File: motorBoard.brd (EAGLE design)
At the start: 127 x 76.3 mm, 74 parts

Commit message: Fixed Git Issues
If this push works, this should be the end of the git-astrophe.
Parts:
- removed C3: 0.1uF, eagle-ltspice:C1206
- moved C8 20.5 mm to (73.4, 9.40)
- moved OSC 19.3 mm to (68.1, 7.62), turned to 270 degrees
- moved C2 16.2 mm to (80.0, 19.7), turned to 0 degrees
- moved C1 2.67 mm to (95.2, 6.48)
- moved C6 1.52 mm to (93.2, 24.0)
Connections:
- net +3V3: now also U$1.73, U$1.74, U$1.75; no longer C3.2
- net +5V: now also U$1.1, U$1.2, U$1.3
- net GNDA: now also U$1.4, U$1.5, U$1.6, U$1.76, U$1.77, U$1.78; no longer C3.1
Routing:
- net MOTOR2A1: track 168.3 -> 105.2 mm, vias 4 -> 3
- net BASIC_HEADER1-4: track 141.6 -> 79.5 mm, vias 5 -> 4
- net MOTOR2LIMB: track 118.0 -> 62.2 mm, vias 2 -> 3
- net MOTOR1POT: track 138.4 -> 89.5 mm, vias 3 -> 4
- net BASIC_HEADER1-5: track 127.2 -> 81.3 mm
- net BASIC_HEADER2-2: track 128.4 -> 91.6 mm, vias 3 -> 4
- net BASIC_HEADER2-4: track 130.3 -> 95.5 mm
- net +5V: track 360.3 -> 326.3 mm, vias 12 -> 8
- net BASIC_HEADER2-6: track 136.7 -> 109.6 mm, vias 9 -> 4
- net BASIC_HEADER2-3: track 118.7 -> 93.4 mm
- net MOTOR4LIMA: track 43.6 -> 68.5 mm, vias 1 -> 2
- net MOTOR1LIMA: track 111.6 -> 88.7 mm, vias 2 -> 3
- net MOTOR4A1: track 82.5 -> 62.0 mm, vias 1 -> 3
- net MOTOR4LIMB: track 36.8 -> 55.6 mm
- net +3V3: track 485.1 -> 503.4 mm, vias 5 -> 2
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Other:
- board text added: "3.3V"
- board text added: "5V"
- board text added: "GND"

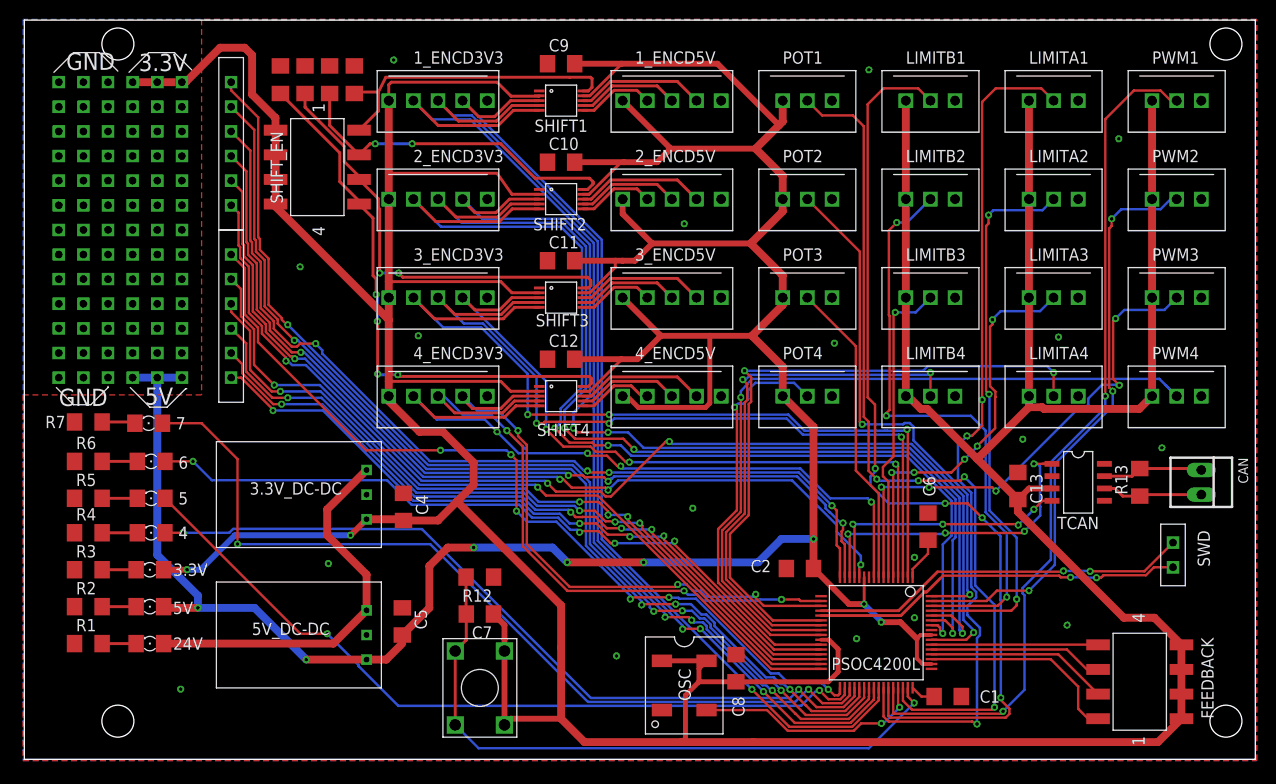
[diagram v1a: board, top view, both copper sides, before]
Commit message: Mostly done with the small board
Removed 1 motor channel, all 3V3 encoders, level shifter enable switches, 1 gpio header. Moved around a ton of components.
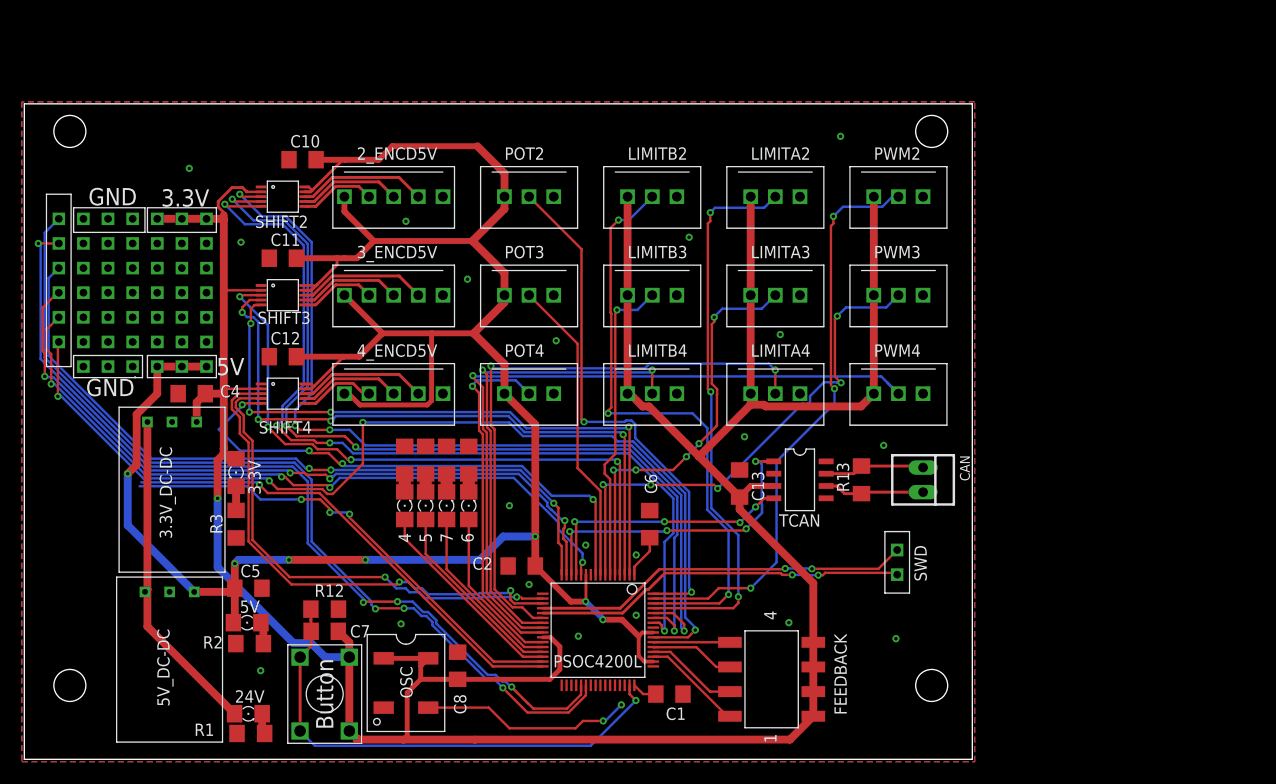
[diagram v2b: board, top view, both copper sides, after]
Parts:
- removed 1_ENCD3V3, 1_ENCD5V, 2_ENCD3V3, 3_ENCD3V3, 4_ENCD3V3: MOLEX5, HuskyRobotics2017-18:MOLEX22-23-2051
- removed BASIC_HEADER1: 6BASIC_HEADER, HuskyRobotics2017-18:6SIP_HEADER
- removed C9: 0.1uF, eagle-ltspice:C1206
- removed LIMITA1, LIMITB1, POT1, PWM1: MOLEX3, HuskyRobotics2017-18:MOLEX22-23-2031
- removed R10, R11, R8, R9: 4.7k, eagle-ltspice:R1206
- removed SHIFT1: LEVEL-SHIFTER_NVT2003DPNVT_2003DP_LEVEL_SHIFTER, HuskyRobotics2017-18:TSSOP10
- removed SHIFT_EN: SMD4SWSMD4SW, HuskyRobotics2017-18:GULL8
- removed U$2: PUSH_BUTTON, HuskyRobotics2017-18:PUSH_BUTTON
- added BUTTON: PUSH_BUTTON, HuskyRobotics2017-18:PUSH_BUTTON
- U$1: value OOPS_SPACE -> OOPS_SPACESMALL; device HuskyRobotics2017-18:OOPS_SPACE -> HuskyRobotics2017-18:OOPS_SPACE_SMALL
- moved R6 39.2 mm to (45.8, 30.9), turned to 270 degrees
- moved FEEDBACK 38.0 mm to (77.1, 8.26)
- moved R7 37.2 mm to (43.6, 30.9), turned to 270 degrees
- moved R5 35.0 mm to (41.4, 30.9), turned to 270 degrees
- moved R4 33.5 mm to (39.2, 30.9), turned to 270 degrees
- moved 6 33.1 mm to (45.8, 26.2), turned to 90 degrees
- moved 7 31.9 mm to (43.6, 26.2), turned to 90 degrees
- moved CAN 28.7 mm to (92.7, 28.8)
- moved 2_ENCD5V 28.7 mm to (38.1, 58.0)
- moved 3_ENCD5V 28.7 mm to (38.1, 47.9)
- moved 4_ENCD5V 28.7 mm to (38.1, 37.7)
- moved C2 28.7 mm to (51.3, 19.9)
- moved C8 28.7 mm to (44.7, 9.65)
- moved OSC 28.7 mm to (39.4, 7.87)
- moved POT2 28.7 mm to (52.1, 58.0)
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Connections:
- removed net BASIC_HEADER1-1: BASIC_HEADER1.1, PSOC4200L.28
- removed net BASIC_HEADER1-2: BASIC_HEADER1.2, PSOC4200L.29
- removed net BASIC_HEADER1-3: BASIC_HEADER1.3, PSOC4200L.30
- removed net BASIC_HEADER1-6: BASIC_HEADER1.6, PSOC4200L.33
- removed net LEVEL_SHIFT_EN1: R11.2, SHIFT1.10, SHIFT_EN.8
- removed net LEVEL_SHIFT_EN2: R10.2, SHIFT2.10, SHIFT_EN.7
- removed net LEVEL_SHIFT_EN3: R9.2, SHIFT3.10, SHIFT_EN.6
- removed net LEVEL_SHIFT_EN4: R8.2, SHIFT4.10, SHIFT_EN.5
- removed net MOTOR1A1: 1_ENCD3V3.4, PSOC4200L.41, SHIFT1.3
- removed net MOTOR1A2: 1_ENCD3V3.3, PSOC4200L.40, SHIFT1.4
- removed net MOTOR1A3: 1_ENCD3V3.2, PSOC4200L.39, SHIFT1.5
- removed net MOTOR1B1: 1_ENCD5V.4, SHIFT1.8
- removed net MOTOR1B2: 1_ENCD5V.3, SHIFT1.7
- removed net MOTOR1B3: 1_ENCD5V.2, SHIFT1.6
- removed net MOTOR1LIMA: LIMITA1.2, PSOC4200L.42
- removed net MOTOR1LIMB: LIMITB1.2, PSOC4200L.43
- removed net MOTOR1POT: POT1.2, PSOC4200L.46
- removed net MOTOR1PWM: PSOC4200L.44, PWM1.2
- net +3V3: now also BUTTON.B1, BUTTON.B2, U$1.37, U$1.38, U$1.39; no longer 1_ENCD3V3.1, 2_ENCD3V3.1, 3_ENCD3V3.1, 4_ENCD3V3.1, LIMITA1.1, LIMITB1.1, PWM1.1, SHIFT1.2, SHIFT_EN.1, SHIFT_EN.2, SHIFT_EN.3, SHIFT_EN.4, U$1.73, U$1.74, U$1.75, U$2.B1, U$2.B2
- net +5V: now also SHIFT2.10, SHIFT3.10, SHIFT4.10; no longer 1_ENCD5V.1, C9.2, POT1.1, SHIFT1.9
- net BASIC_HEADER1-4: no longer BASIC_HEADER1.4
- net BASIC_HEADER1-5: no longer BASIC_HEADER1.5
- net CLK_EXT: no longer PSOC4200L.45
- net GNDA: now also U$1.40, U$1.41, U$1.42; no longer 1_ENCD3V3.5, 1_ENCD5V.5, 2_ENCD3V3.5, 3_ENCD3V3.5, 4_ENCD3V3.5, C9.1, LIMITA1.3, LIMITB1.3, POT1.3, PWM1.3, R10.1, R11.1, R8.1, R9.1, SHIFT1.1, U$1.76, U$1.77, U$1.78
- net LED4: now also PSOC4200L.30; no longer PSOC4200L.36
- net LED5: now also PSOC4200L.29; no longer PSOC4200L.34
- net LED7: now also PSOC4200L.28; no longer PSOC4200L.35
- net MOTOR2A1: no longer 2_ENCD3V3.4
- net MOTOR2A2: no longer 2_ENCD3V3.3
- net MOTOR2A3: no longer 2_ENCD3V3.2
- net MOTOR3A1: no longer 3_ENCD3V3.4
- net MOTOR3A2: no longer 3_ENCD3V3.3
- net MOTOR3A3: no longer 3_ENCD3V3.2
- net MOTOR4A1: no longer 4_ENCD3V3.4
- net MOTOR4A2: no longer 4_ENCD3V3.3
- net MOTOR4A3: no longer 4_ENCD3V3.2
- net XRES: now also BUTTON.A1, BUTTON.A2; no longer U$2.A1, U$2.A2
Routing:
- net +3V3: track 503.4 -> 304.2 mm, vias 2 -> 1
- net MOTOR1A3: track 108.8 -> 0.00 mm, vias 3 -> 0
- net MOTOR1A2: track 104.1 -> 0.00 mm, vias 3 -> 0
- net MOTOR1A1: track 99.5 -> 0.00 mm, vias 1 -> 0
- net MOTOR1LIMB: track 97.5 -> 0.00 mm, vias 4 -> 0
- net MOTOR1POT: track 89.5 -> 0.00 mm, vias 4 -> 0
- net BASIC_HEADER1-6: track 89.4 -> 0.00 mm, vias 6 -> 0
- net MOTOR1PWM: track 88.7 -> 0.00 mm, vias 2 -> 0
- net MOTOR1LIMA: track 88.7 -> 0.00 mm, vias 3 -> 0
- net BASIC_HEADER1-3: track 76.9 -> 0.00 mm, vias 4 -> 0
- net +5V: track 326.3 -> 251.2 mm, vias 8 -> 7
- net BASIC_HEADER1-2: track 74.5 -> 0.00 mm, vias 4 -> 0
- net BASIC_HEADER1-1: track 72.8 -> 0.00 mm, vias 4 -> 0
- net LED7: track 90.2 -> 18.4 mm, vias 2 -> 0
- net LED5: track 81.0 -> 19.8 mm, vias 2 -> 0
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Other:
- board size 127 x 76.3 mm -> 97.8 x 67.6 mm
- board text added: "Button"
- board text removed: "R8...11"

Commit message: "Done" except for silk screen and DFM check
Added 24V terminal blocks, second CAN header, limit switch debounces.
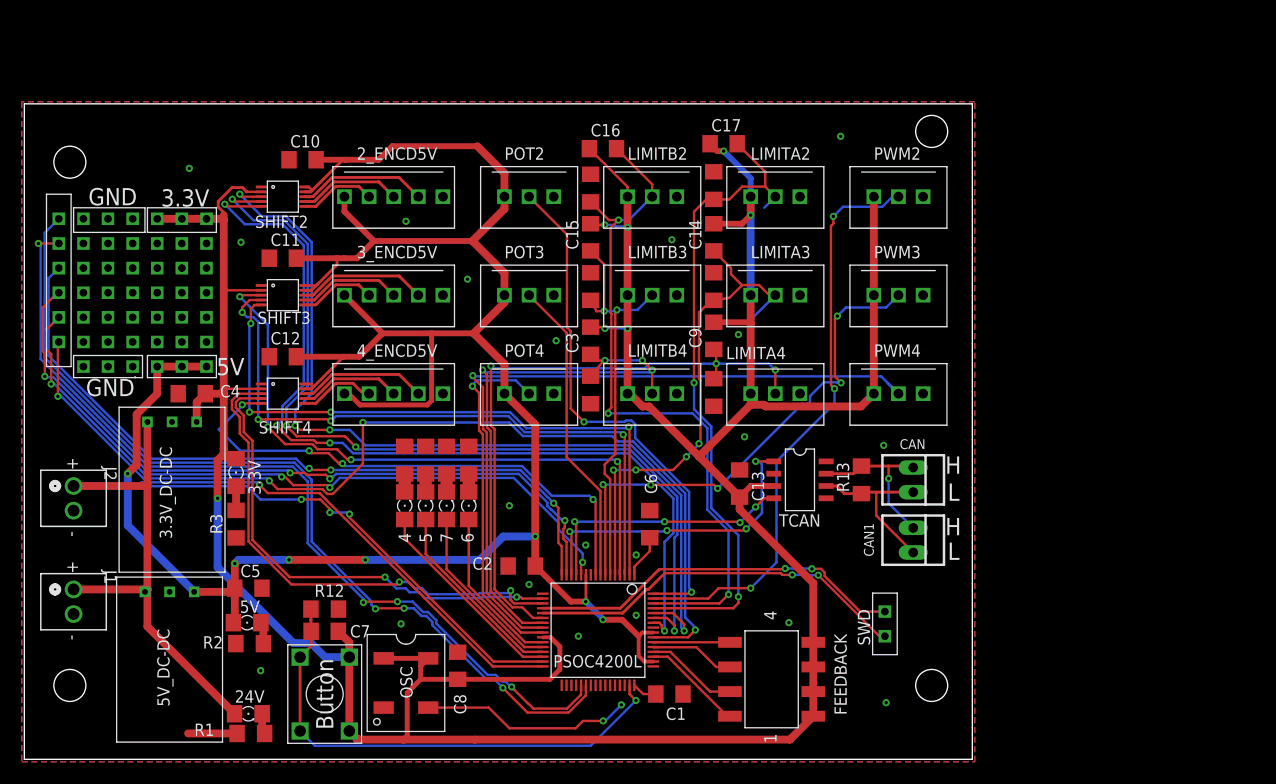
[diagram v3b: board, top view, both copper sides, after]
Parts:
- added C14, C15, C16, C17, C3, C9: 0.1uF, eagle-ltspice:C1206
- added CAN1: 22-23-2021, con-molex:22-23-2021
- added J1, J2: TE-TERM-BLOCK, HuskyRobotics17-18:TE-TERM-BLOCK
- added R10, R11, R14, R15, R8, R9: 1k, eagle-ltspice:R1206
- moved SWD 6.48 mm to (88.8, 14.0)
- moved CAN 1.02 mm to (91.7, 28.8)
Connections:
- net +24V: now also J1.L, J2.L
- net +3V3: now also C14.2, C15.2, C16.1, C17.1, C3.2, C9.2
- net CANH: now also CAN1.1
- net CANL: now also CAN1.2
- net GNDA: now also J1.R, J2.R, R10.1, R11.1, R14.1, R15.1, R8.1, R9.1
- net MOTOR2LIMA: now also C17.2, R14.2
- net MOTOR2LIMB: now also C16.2, R15.2
- net MOTOR3LIMA: now also C14.1, R11.2
- net MOTOR3LIMB: now also C15.1, R10.2
- net MOTOR4LIMA: now also C9.1, R9.2
- net MOTOR4LIMB: now also C3.1, R8.2
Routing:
- net +3V3: track 304.2 -> 334.3 mm, vias 1 -> 7
- net +24V: track 34.2 -> 49.5 mm
- net MOTOR3LIMA: track 42.3 -> 52.7 mm, vias 5 -> 4
- net MOTOR2LIMA: track 58.1 -> 68.4 mm, vias 3 -> 2
- net MOTOR3LIMB: track 32.3 -> 42.6 mm, vias 1 -> 2
- net MOTOR2LIMB: track 62.2 -> 72.3 mm
- net MOTOR4LIMB: track 50.0 -> 59.3 mm, vias 2 -> 4
- net CANL: track 10.4 -> 17.2 mm
- net CANH: track 10.4 -> 17.2 mm, vias 0 -> 1
- net GNDA: track 0.00 -> 5.06 mm
- net MOTOR4LIMA: track 61.7 -> 65.0 mm, vias 2 -> 3
- net SWD_CLK: track 38.5 -> 39.7 mm
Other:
- board text added: "H"
- board text added: "L"

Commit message: Finished Silk Screening
Ready for DFM test!
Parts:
- removed 6: (no value), eagle-ltspice:LED_1206
- removed LIMITA4, LIMITB4, POT4, PWM4: MOLEX3, HuskyRobotics2017-18:MOLEX22-23-2031
- added 1: (no value), eagle-ltspice:LED_1206
- added LIMITA1, LIMITB1, POT1, PWM1: MOLEX3, HuskyRobotics2017-18:MOLEX22-23-2031
- moved LIMITA2 10.2 mm to (77.5, 47.9)
- moved LIMITB2 10.2 mm to (64.8, 47.9)
- moved POT2 10.2 mm to (52.1, 47.9)
- moved PWM2 10.2 mm to (90.2, 47.9)
- moved LIMITA3 10.2 mm to (77.5, 37.7)
- moved LIMITB3 10.2 mm to (64.8, 37.7)
- moved POT3 10.2 mm to (52.1, 37.7)
- moved PWM3 10.2 mm to (90.2, 37.7)
- moved 4 6.60 mm to (45.8, 26.2)
- renumbered 2_ENCD5V to ENCD1, 3_ENCD5V to ENCD2, 4_ENCD5V to ENCD3, 5 to 2, 7 to 3, OSC to OSC_EXT
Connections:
- net +3V3: now also LIMITA1.1, LIMITB1.1, PWM1.1; no longer LIMITA4.1, LIMITB4.1, PWM4.1
- net +5V: now also POT1.1; no longer POT4.1
- net GNDA: now also LIMITA1.3, LIMITB1.3, POT1.3, PWM1.3; no longer LIMITA4.3, LIMITB4.3, POT4.3, PWM4.3
- net LED4: now also 1.A; no longer 4.A
- net LED6: now also 4.A; no longer 6.A
- net MOTOR2LIMA: now also LIMITA1.2; no longer LIMITA2.2
- net MOTOR2LIMB: now also LIMITB1.2; no longer LIMITB2.2
- net MOTOR2POT: now also POT1.2; no longer POT2.2
- net MOTOR2PWM: now also PWM1.2; no longer PWM2.2
- net MOTOR3LIMA: now also LIMITA2.2; no longer LIMITA3.2
- net MOTOR3LIMB: now also LIMITB2.2; no longer LIMITB3.2
- net MOTOR3POT: now also POT2.2; no longer POT3.2
- net MOTOR3PWM: now also PWM2.2; no longer PWM3.2
- net MOTOR4LIMA: now also LIMITA3.2; no longer LIMITA4.2
- net MOTOR4LIMB: now also LIMITB3.2; no longer LIMITB4.2
- net MOTOR4POT4: now also POT3.2; no longer POT4.2
- net MOTOR4PWM: now also PWM3.2; no longer PWM4.2
- net N$10: now also 1.C; no longer 4.C
- net N$17: now also 4.C; no longer 6.C
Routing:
- net GNDA: track 5.06 -> 0.00 mm
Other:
- board size 97.8 x 67.6 mm -> 97.8 x 68.6 mm
- board text added: "24V"
- board text added: "5.5"
- board text added: "6.0"
- board text added: "6.4"
- board text added: "6.5"
- board text added: "7.0"
- board text added: "7.1"
- board text added: "All LIMIT caps are 0.1uF, resistors are 1k"
- board text added: "All connectors, PWR Left, GND Right"
- board text added: "Husky Robotics 2017-18 | Arm Motor Board Dylan Tomberlin | tomberln@uw.edu"
- board text added: "R"
- board text added: "Switch"

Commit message: Made changes for Bay Area Circuits DFM
Re-Zipped
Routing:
- net GNDA: track 0.00 -> 0.63 mm
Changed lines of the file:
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@@
 <setting verticaltext="up"/>
 </settings>
-<grid distance="0.000000123031" unitdist="inch" unit="inch" style="lines" multiple="1" display="no" altdistance="0.125" altunitdist="inch" altunit="inch"/>
+<grid distance="10" unitdist="mil" unit="mil" style="dots" multiple="1" display="yes" altdistance="0.125" altunitdist="inch" altunit="inch"/>
 <layers>
 <layer number="1" name="Top" color="4" fill="1" visible="yes" active="yes"/>
@@
 <via x="56.7744" y="24.511" extent="1-16" drill="0.35"/>
 <via x="75.438" y="26.035" extent="1-16" drill="0.35"/>
-<wire x1="73.822940625" y1="24.419940625" x2="75.438" y2="26.035" width="0.254" layer="16"/>
 <wire x1="75.438" y1="26.035" x2="76.327" y2="26.924" width="0.254" layer="1"/>
 <wire x1="76.327" y1="26.924" x2="77.31" y2="26.924" width="0.254" layer="1"/>
 <wire x1="56.7744" y1="24.511" x2="66.04" y2="24.511" width="0.254" layer="16"/>
 <via x="66.04" y="24.511" extent="1-16" drill="0.35"/>
-<wire x1="73.73188125" y1="24.511" x2="66.04" y2="24.511" width="0.254" layer="1"/>
-<wire x1="73.73188125" y1="24.511" x2="73.822940625" y2="24.419940625" width="0.254" layer="1"/>
-<via x="73.822940625" y="24.419940625" extent="1-16" drill="0.35"/>
+<wire x1="75.438" y1="26.035" x2="73.914" y2="24.511" width="0.254" layer="16"/>
+<wire x1="73.914" y1="24.511" x2="73.279" y2="24.511" width="0.254" layer="16"/>
+<via x="73.279" y="24.511" extent="1-16" drill="0.35"/>
+<wire x1="73.279" y1="24.511" x2="66.04" y2="24.511" width="0.254" layer="1"/>
 </signal>
 <signal name="CANTX">
@@
 <wire x1="66.1868" y1="23.495" x2="66.294" y2="23.6022" width="0.254" layer="16"/>
 <via x="66.294" y="23.6022" extent="1-16" drill="0.35"/>
-<wire x1="66.294" y1="23.6022" x2="74.29044375" y2="23.6022" width="0.254" layer="1"/>
-<wire x1="74.29044375" y1="23.6022" x2="74.4655625" y2="23.77731875" width="0.254" layer="1"/>
-<via x="74.4655625" y="23.77731875" extent="1-16" drill="0.35"/>
-<wire x1="74.4655625" y1="23.77731875" x2="76.0956" y2="25.40735625" width="0.254" layer="16"/>
 <wire x1="76.0956" y1="25.40735625" x2="76.0956" y2="26.3073875" width="0.254" layer="16"/>
 <wire x1="76.327" y1="30.734" x2="77.31" y2="30.734" width="0.254" layer="1"/>
@@
 <via x="75.438" y="30.734" extent="1-16" drill="0.35"/>
 <wire x1="75.438" y1="30.734" x2="77.31" y2="30.734" width="0.254" layer="1"/>
+<wire x1="66.294" y1="23.6022" x2="74.1017875" y2="23.6022" width="0.254" layer="1"/>
+<wire x1="74.1017875" y1="23.6022" x2="74.19285" y2="23.5111375" width="0.254" layer="1"/>
+<via x="74.19285" y="23.5111375" extent="1-16" drill="0.35"/>
+<wire x1="74.19285" y1="23.5111375" x2="76.08906875" y2="25.40735625" width="0.254" layer="16"/>
+<wire x1="76.08906875" y1="25.40735625" x2="76.0956" y2="25.40735625" width="0.254" layer="16"/>
 </signal>
 <signal name="+5V">
@@
 <via x="52.07" y="18.034" extent="1-16" drill="0.35"/>
 <via x="24.384" y="9.144" extent="1-16" drill="0.35"/>
-<polygon width="0.1524" layer="1">
-<vertex x="-0.254" y="-0.254"/>
-<vertex x="98.044" y="-0.254"/>
-<vertex x="98.044" y="67.818"/>
-<vertex x="-0.254" y="67.818"/>
-</polygon>
-<polygon width="0.1524" layer="16">
-<vertex x="-0.254" y="-0.254"/>
-<vertex x="98.044" y="-0.254"/>
-<vertex x="98.044" y="67.818"/>
-<vertex x="-0.254" y="67.818"/>
-</polygon>
 <contactref element="J1" pad="R"/>
 <contactref element="J2" pad="R"/>
@@
 <contactref element="R14" pad="1"/>
 <contactref element="R15" pad="1"/>
+<wire x1="24.42" y1="38.719" x2="24.2703375" y2="38.8686625" width="0.254" layer="1"/>
+<wire x1="24.2703375" y1="38.8686625" x2="24.2703375" y2="39.28686875" width="0.254" layer="1"/>
+<polygon width="0.1524" layer="1">
+<vertex x="-0.508" y="-0.508"/>
+<vertex x="98.298" y="-0.508"/>
+<vertex x="98.298" y="69.342"/>
+<vertex x="-0.508" y="69.342"/>
+</polygon>
+<polygon width="0.1524" layer="16">
+<vertex x="-0.254" y="-0.508"/>
+<vertex x="98.298" y="-0.508"/>
+<vertex x="98.298" y="69.088"/>
+<vertex x="-0.508" y="69.088"/>
+<vertex x="-0.508" y="-0.508"/>
+</polygon>
 </signal>
 <signal name="+3V3">
@@
 <wire x1="54.2817375" y1="12.585" x2="55.245" y2="11.6217375" width="0.508" layer="1"/>
 <wire x1="53.482" y1="12.585" x2="54.2817375" y2="12.585" width="0.4064" layer="1"/>
-<wire x1="73.787" y1="27.048" x2="74.933" y2="28.194" width="0.6096" layer="1"/>
-<wire x1="74.933" y1="28.194" x2="77.31" y2="28.194" width="0.6096" layer="1"/>
 <wire x1="22.995" y1="58.539" x2="24.42" y2="58.539" width="0.254" layer="1"/>
 <wire x1="20.5640125" y1="31.4860125" x2="20.5640125" y2="32.05911875" width="0.8128" layer="1"/>
@@
 <wire x1="71.12" y1="45.088" x2="74.8" y2="45.088" width="0.6096" layer="1"/>
 <wire x1="74.8" y1="45.088" x2="74.93" y2="44.958" width="0.6096" layer="1"/>
+<wire x1="73.787" y1="27.048" x2="74.8003625" y2="28.0613625" width="0.6096" layer="1"/>
+<wire x1="77.1773625" y1="28.0613625" x2="77.31" y2="28.194" width="0.6096" layer="1"/>
+<wire x1="74.8003625" y1="28.0613625" x2="77.1773625" y2="28.0613625" width="0.6096" layer="1"/>
 </signal>
 <signal name="SEL_SW3">
@@
 <wire x1="22.117275" y1="37.719" x2="21.415" y2="37.016725" width="0.254" layer="1"/>
 <wire x1="21.415" y1="37.016725" x2="21.415" y2="36.115475" width="0.254" layer="1"/>
-<via x="50.1723625" y="17.4002" extent="1-16" drill="0.35"/>
-<wire x1="50.5276125" y1="16.085" x2="50.1424" y2="16.4702125" width="0.254" layer="1"/>
-<wire x1="50.1424" y1="16.4702125" x2="50.1424" y2="17.0149875" width="0.254" layer="1"/>
-<wire x1="50.1424" y1="17.0149875" x2="50.1723625" y2="17.04495" width="0.254" layer="1"/>
-<wire x1="50.1723625" y1="17.04495" x2="50.1723625" y2="17.4002" width="0.254" layer="1"/>
 <wire x1="53.482" y1="16.085" x2="50.5276125" y2="16.085" width="0.254" layer="1"/>
-<wire x1="50.1723625" y1="17.4002" x2="49.9211625" y2="17.149" width="0.254" layer="16"/>
-<wire x1="49.9211625" y1="17.149" x2="46.96825" y2="17.149" width="0.254" layer="16"/>
-<wire x1="46.96825" y1="17.149" x2="46.8433625" y2="17.0241125" width="0.254" layer="16"/>
 <wire x1="46.8433625" y1="17.0241125" x2="41.6498875" y2="17.0241125" width="0.254" layer="16"/>
+<wire x1="49.827371875" y1="16.785240625" x2="49.827371875" y2="17.4002" width="0.254" layer="1"/>
+<via x="49.827371875" y="17.4002" extent="1-16" drill="0.35"/>
+<wire x1="49.827371875" y1="17.4002" x2="47.21945" y2="17.4002" width="0.254" layer="16"/>
+<wire x1="50.5276125" y1="16.085" x2="49.827371875" y2="16.785240625" width="0.254" layer="1"/>
+<wire x1="47.21945" y1="17.4002" x2="46.8433625" y2="17.0241125" width="0.254" layer="16"/>
 </signal>
 <signal name="MOTOR4LIMB">
